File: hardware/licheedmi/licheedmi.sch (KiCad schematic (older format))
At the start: 74 parts, among them J1 Conn_01x09, J2 HDMI_A_PCB, J3 LicheePiNano_LCD, J4 HDMI_A, J5 USB_C_Receptacle_USB2.0, U1 TDA19988, U2 LicheeNano, U3 TS3DV20812, U4 SC6206B, U5 CH340C

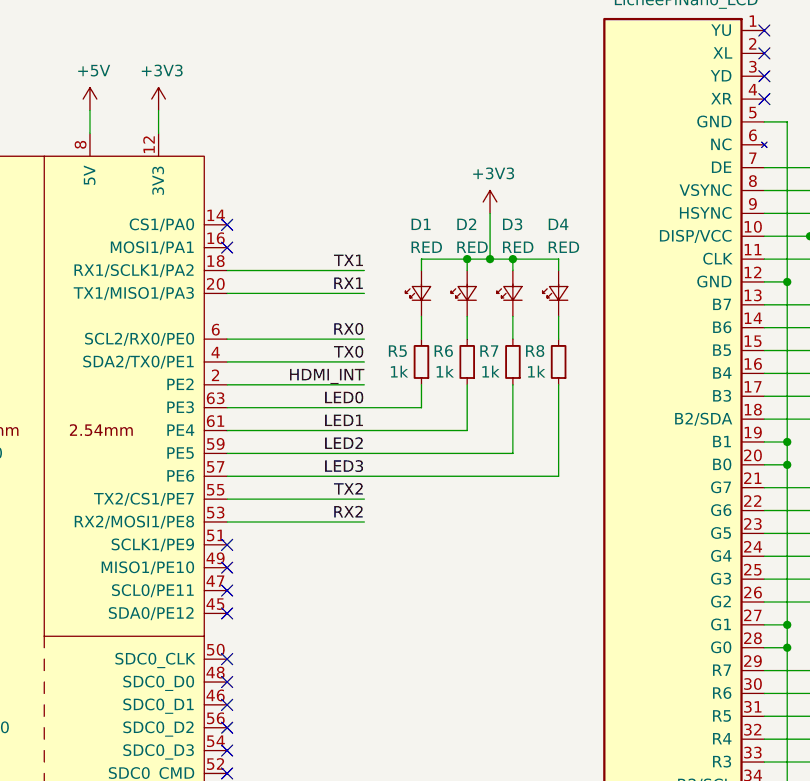
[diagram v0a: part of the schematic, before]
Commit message: pcb: Reroute PCB following footprint flip
Bowtie and complicated via thingies are gone now \o/
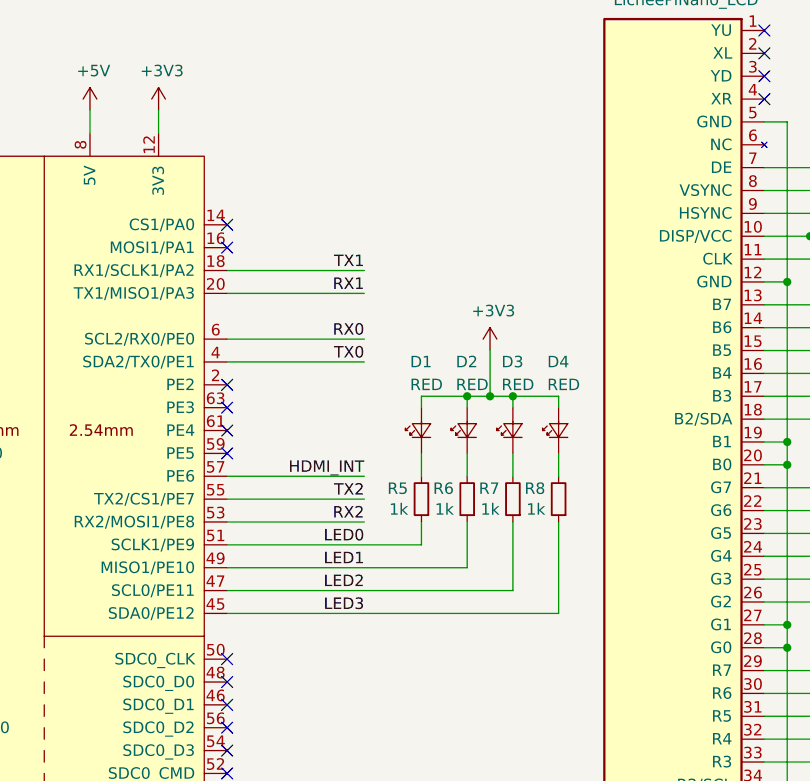
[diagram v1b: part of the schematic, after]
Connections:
- net HDMI_INT: now also U2.57 (PE6); no longer U2.2 (PE2)
- net LED0: now also U2.51 (SCLK1/PE9); no longer U2.63 (PE3)
- net LED1: now also U2.49 (MISO1/PE10); no longer U2.61 (PE4)
- net LED2: now also U2.47 (SCL0/PE11); no longer U2.59 (PE5)
- net LED3: now also U2.45 (SDA0/PE12); no longer U2.57 (PE6)
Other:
- moved on the sheet: D1, D2, D3, D4, R5, R6, R7, R8
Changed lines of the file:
@@
 Wire Wire Line
 	9300 2650 9950 2650
-$Comp
-L hdmizness:LicheeNano U2
-U 1 1 5F223DE5
-P 1750 2600
-F 0 "U2" H 2700 -1000 50  0000 C CNN
-F 1 "LicheeNano" H 2850 -1100 50  0000 C CNN
-F 2 "hdmizness:LicheeNano" H 1500 2650 50  0001 C CNN
-F 3 "${KIPRJMOD}/../../documentation/lichee_nano_8.16_schematic.pdf" H 1500 2650 50  0001 C CNN
-F 4 "C35445" H 1750 2600 50  0001 C CNN "LCSC P/N"
-F 5 "C35445" H 1750 2600 50  0001 C CNN "MFR P/N"
-	1    1750 2600
-	1    0    0    -1
-$EndComp
 Text Label 6200 3650 2    50   ~ 0
 LCD_B3
@@
 RX0
 Wire Wire Line
-	3250 3600 3850 3600
-Text Label 3850 3600 2    50   ~ 0
+	3250 4000 3850 4000
+Text Label 3850 4000 2    50   ~ 0
 HDMI_INT
 $Comp
@@
 Text Label 3850 3200 2    50   ~ 0
 RX1
-Text Label 3850 4000 2    50   ~ 0
+Text Label 3850 4600 2    50   ~ 0
 LED3
-Text Label 3850 3900 2    50   ~ 0
+Text Label 3850 4500 2    50   ~ 0
 LED2
-Text Label 3850 3700 2    50   ~ 0
+Text Label 3850 4300 2    50   ~ 0
 LED0
-Text Label 3850 3800 2    50   ~ 0
+Text Label 3850 4400 2    50   ~ 0
 LED1
 Wire Wire Line
@@
 L Device:R_Small R8
 U 1 1 5F6D2F20
-P 4700 3500
-F 0 "R8" H 4758 3454 50  0000 L CNN
-F 1 "1k" H 4758 3545 50  0000 L CNN
-F 2 "Resistor_SMD:R_0603_1608Metric" H 4700 3500 50  0001 C CNN
-F 3 "~" H 4700 3500 50  0001 C CNN
-F 4 "C380759" H 4700 3500 50  0001 C CNN "LCSC P/N"
-F 5 "SY0603JN1KP" H 4700 3500 50  0001 C CNN "MFR P/N"
-	1    4700 3500
+P 4700 4100
+F 0 "R8" H 4758 4054 50  0000 L CNN
+F 1 "1k" H 4758 4145 50  0000 L CNN
+F 2 "Resistor_SMD:R_0603_1608Metric" H 4700 4100 50  0001 C CNN
+F 3 "~" H 4700 4100 50  0001 C CNN
+F 4 "C380759" H 4700 4100 50  0001 C CNN "LCSC P/N"
+F 5 "SY0603JN1KP" H 4700 4100 50  0001 C CNN "MFR P/N"
+	1    4700 4100
 	-1   0    0    1
 $EndComp
 Wire Wire Line
-	4700 3300 4700 3400
-Wire Wire Line
-	4700 3050 4700 3100
+	4700 3900 4700 4000
+Wire Wire Line
+	4700 3650 4700 3700
 $Comp
 L power:+3V3 #PWR07
 U 1 1 5F89613D
-P 4400 2850
-F 0 "#PWR07" H 4400 2700 50  0001 C CNN
-F 1 "+3V3" H 4415 3023 50  0000 C CNN
-F 2 "" H 4400 2850 50  0001 C CNN
-F 3 "" H 4400 2850 50  0001 C CNN
-	1    4400 2850
-	1    0    0    -1
-$EndComp
-Wire Wire Line
-	4400 3050 4500 3050
-Connection ~ 4400 3050
-Wire Wire Line
-	4400 3050 4400 2850
-Wire Wire Line
-	4500 3050 4700 3050
-Connection ~ 4500 3050
-Wire Wire Line
-	4500 3100 4500 3050
-Wire Wire Line
-	4300 3050 4400 3050
-Connection ~ 4300 3050
-Wire Wire Line
-	4300 3100 4300 3050
-Wire Wire Line
-	4100 3050 4300 3050
-Wire Wire Line
-	4100 3100 4100 3050
-Wire Wire Line
-	4500 3300 4500 3400
-Wire Wire Line
-	4300 3300 4300 3400
-Wire Wire Line
-	4100 3300 4100 3400
+P 4400 3450
+F 0 "#PWR07" H 4400 3300 50  0001 C CNN
+F 1 "+3V3" H 4415 3623 50  0000 C CNN
+F 2 "" H 4400 3450 50  0001 C CNN
+F 3 "" H 4400 3450 50  0001 C CNN
+	1    4400 3450
+	1    0    0    -1
+$EndComp
+Wire Wire Line
+	4400 3650 4500 3650
+Connection ~ 4400 3650
+Wire Wire Line
+	4400 3650 4400 3450
+Wire Wire Line
+	4500 3650 4700 3650
+Connection ~ 4500 3650
+Wire Wire Line
+	4500 3700 4500 3650
+Wire Wire Line
+	4300 3650 4400 3650
+Connection ~ 4300 3650
+Wire Wire Line
+	4300 3700 4300 3650
+Wire Wire Line
+	4100 3650 4300 3650
+Wire Wire Line
+	4100 3700 4100 3650
+Wire Wire Line
+	4500 3900 4500 4000
+Wire Wire Line
+	4300 3900 4300 4000
+Wire Wire Line
+	4100 3900 4100 4000
 $Comp
 L Device:LED_Small D1
 U 1 1 5F6D3496
-P 4100 3200
-F 0 "D1" V 4400 3250 50  0000 R CNN
-F 1 "RED" V 4300 3250 50  0000 R CNN
-F 2 "LED_SMD:LED_0603_1608Metric" V 4100 3200 50  0001 C CNN
-F 3 "~" V 4100 3200 50  0001 C CNN
-F 4 "C157741" H 4100 3200 50  0001 C CNN "LCSC P/N"
-F 5 "LTST-C193KRKT-5A" H 4100 3200 50  0001 C CNN "MFR P/N"
-	1    4100 3200
+P 4100 3800
+F 0 "D1" V 4400 3850 50  0000 R CNN
+F 1 "RED" V 4300 3850 50  0000 R CNN
+F 2 "LED_SMD:LED_0603_1608Metric" V 4100 3800 50  0001 C CNN
+F 3 "~" V 4100 3800 50  0001 C CNN
+F 4 "C157741" H 4100 3800 50  0001 C CNN "LCSC P/N"
+F 5 "LTST-C193KRKT-5A" H 4100 3800 50  0001 C CNN "MFR P/N"
+	1    4100 3800
 	0    -1   -1   0
 $EndComp
@@
 L Device:R_Small R7
 U 1 1 5F6D2C74
-P 4500 3500
-F 0 "R7" H 4558 3454 50  0000 L CNN
-F 1 "1k" H 4558 3545 50  0000 L CNN
-F 2 "Resistor_SMD:R_0603_1608Metric" H 4500 3500 50  0001 C CNN
-F 3 "~" H 4500 3500 50  0001 C CNN
-F 4 "C380759" H 4500 3500 50  0001 C CNN "LCSC P/N"
-F 5 "SY0603JN1KP" H 4500 3500 50  0001 C CNN "MFR P/N"
-	1    4500 3500
+P 4500 4100
+F 0 "R7" H 4558 4054 50  0000 L CNN
+F 1 "1k" H 4558 4145 50  0000 L CNN
+F 2 "Resistor_SMD:R_0603_1608Metric" H 4500 4100 50  0001 C CNN
+F 3 "~" H 4500 4100 50  0001 C CNN
+F 4 "C380759" H 4500 4100 50  0001 C CNN "LCSC P/N"
+F 5 "SY0603JN1KP" H 4500 4100 50  0001 C CNN "MFR P/N"
+	1    4500 4100
 	-1   0    0    1
 $EndComp
@@
 L Device:R_Small R6
 U 1 1 5F6D21F3
-P 4300 3500
-F 0 "R6" H 4358 3454 50  0000 L CNN
-F 1 "1k" H 4358 3545 50  0000 L CNN
-F 2 "Resistor_SMD:R_0603_1608Metric" H 4300 3500 50  0001 C CNN
-F 3 "~" H 4300 3500 50  0001 C CNN
-F 4 "C380759" H 4300 3500 50  0001 C CNN "LCSC P/N"
-F 5 "SY0603JN1KP" H 4300 3500 50  0001 C CNN "MFR P/N"
-	1    4300 3500
+P 4300 4100
+F 0 "R6" H 4358 4054 50  0000 L CNN
+F 1 "1k" H 4358 4145 50  0000 L CNN
+F 2 "Resistor_SMD:R_0603_1608Metric" H 4300 4100 50  0001 C CNN
+F 3 "~" H 4300 4100 50  0001 C CNN
+F 4 "C380759" H 4300 4100 50  0001 C CNN "LCSC P/N"
+F 5 "SY0603JN1KP" H 4300 4100 50  0001 C CNN "MFR P/N"
+	1    4300 4100
 	-1   0    0    1
 $EndComp
@@
 L Device:R_Small R5
 U 1 1 5F6D0AA1
-P 4100 3500
-F 0 "R5" H 4158 3454 50  0000 L CNN
-F 1 "1k" H 4158 3545 50  0000 L CNN
-F 2 "Resistor_SMD:R_0603_1608Metric" H 4100 3500 50  0001 C CNN
-F 3 "~" H 4100 3500 50  0001 C CNN
-F 4 "C380759" H 4100 3500 50  0001 C CNN "LCSC P/N"
-F 5 "SY0603JN1KP" H 4100 3500 50  0001 C CNN "MFR P/N"
-	1    4100 3500
+P 4100 4100
+F 0 "R5" H 4158 4054 50  0000 L CNN
+F 1 "1k" H 4158 4145 50  0000 L CNN
+F 2 "Resistor_SMD:R_0603_1608Metric" H 4100 4100 50  0001 C CNN
+F 3 "~" H 4100 4100 50  0001 C CNN
+F 4 "C380759" H 4100 4100 50  0001 C CNN "LCSC P/N"
+F 5 "SY0603JN1KP" H 4100 4100 50  0001 C CNN "MFR P/N"
+	1    4100 4100
 	-1   0    0    1
 $EndComp
 Wire Wire Line
-	4100 3700 4100 3600
-Wire Wire Line
-	3250 3700 4100 3700
-Wire Wire Line
-	4300 3800 4300 3600
-Wire Wire Line
-	3250 3800 4300 3800
-Wire Wire Line
-	4500 3900 4500 3600
-Wire Wire Line
-	3250 3900 4500 3900
-Wire Wire Line
-	4700 4000 4700 3600
-Wire Wire Line
-	3250 4000 4700 4000
+	4100 4300 4100 4200
+Wire Wire Line
+	3250 4300 4100 4300
+Wire Wire Line
+	4300 4400 4300 4200
+Wire Wire Line
+	3250 4400 4300 4400
+Wire Wire Line
+	4500 4500 4500 4200
+Wire Wire Line
+	3250 4500 4500 4500
+Wire Wire Line
+	4700 4600 4700 4200
+Wire Wire Line
+	3250 4600 4700 4600
 NoConn ~ 3250 2900
-NoConn ~ 3250 3000
-NoConn ~ 3250 4300
-NoConn ~ 3250 4400
-NoConn ~ 3250 4500
-NoConn ~ 3250 4600
+NoConn ~ 3250 3600
 $Comp
 L hdmizness:SC6206B U4
@@
 L Device:LED_Small D2
 U 1 1 613C01A5
-P 4300 3200
-F 0 "D2" V 4600 3250 50  0000 R CNN
-F 1 "RED" V 4500 3250 50  0000 R CNN
-F 2 "LED_SMD:LED_0603_1608Metric" V 4300 3200 50  0001 C CNN
-F 3 "~" V 4300 3200 50  0001 C CNN
-F 4 "C157741" H 4300 3200 50  0001 C CNN "LCSC P/N"
-F 5 "LTST-C193KRKT-5A" H 4300 3200 50  0001 C CNN "MFR P/N"
-	1    4300 3200
+P 4300 3800
+F 0 "D2" V 4600 3850 50  0000 R CNN
+F 1 "RED" V 4500 3850 50  0000 R CNN
+F 2 "LED_SMD:LED_0603_1608Metric" V 4300 3800 50  0001 C CNN
+F 3 "~" V 4300 3800 50  0001 C CNN
+F 4 "C157741" H 4300 3800 50  0001 C CNN "LCSC P/N"
+F 5 "LTST-C193KRKT-5A" H 4300 3800 50  0001 C CNN "MFR P/N"
+	1    4300 3800
 	0    -1   -1   0
 $EndComp
@@
 L Device:LED_Small D3
 U 1 1 613C082E
-P 4500 3200
-F 0 "D3" V 4800 3250 50  0000 R CNN
-F 1 "RED" V 4700 3250 50  0000 R CNN
-F 2 "LED_SMD:LED_0603_1608Metric" V 4500 3200 50  0001 C CNN
-F 3 "~" V 4500 3200 50  0001 C CNN
-F 4 "C157741" H 4500 3200 50  0001 C CNN "LCSC P/N"
-F 5 "LTST-C193KRKT-5A" H 4500 3200 50  0001 C CNN "MFR P/N"
-	1    4500 3200
+P 4500 3800
+F 0 "D3" V 4800 3850 50  0000 R CNN
+F 1 "RED" V 4700 3850 50  0000 R CNN
+F 2 "LED_SMD:LED_0603_1608Metric" V 4500 3800 50  0001 C CNN
+F 3 "~" V 4500 3800 50  0001 C CNN
+F 4 "C157741" H 4500 3800 50  0001 C CNN "LCSC P/N"
+F 5 "LTST-C193KRKT-5A" H 4500 3800 50  0001 C CNN "MFR P/N"
+	1    4500 3800
 	0    -1   -1   0
 $EndComp
@@
 L Device:LED_Small D4
 U 1 1 613C0C7E
-P 4700 3200
-F 0 "D4" V 5000 3250 50  0000 R CNN
-F 1 "RED" V 4900 3250 50  0000 R CNN
-F 2 "LED_SMD:LED_0603_1608Metric" V 4700 3200 50  0001 C CNN
-F 3 "~" V 4700 3200 50  0001 C CNN
-F 4 "C157741" H 4700 3200 50  0001 C CNN "LCSC P/N"
-F 5 "LTST-C193KRKT-5A" H 4700 3200 50  0001 C CNN "MFR P/N"
-	1    4700 3200
+P 4700 3800
+F 0 "D4" V 5000 3850 50  0000 R CNN
+F 1 "RED" V 4900 3850 50  0000 R CNN
+F 2 "LED_SMD:LED_0603_1608Metric" V 4700 3800 50  0001 C CNN
+F 3 "~" V 4700 3800 50  0001 C CNN
+F 4 "C157741" H 4700 3800 50  0001 C CNN "LCSC P/N"
+F 5 "LTST-C193KRKT-5A" H 4700 3800 50  0001 C CNN "MFR P/N"
+	1    4700 3800
 	0    -1   -1   0
 $EndComp
@@
 	5700 2450 5700 3150
 Connection ~ 5700 3150
+$Comp
+L hdmizness:LicheeNano U2
+U 1 1 5F223DE5
+P 1750 2600
+F 0 "U2" H 2700 -1000 50  0000 C CNN
+F 1 "LicheeNano" H 2850 -1100 50  0000 C CNN
+F 2 "hdmizness:LicheeNano" H 1500 2650 50  0001 C CNN
+F 3 "${KIPRJMOD}/../../documentation/lichee_nano_8.16_schematic.pdf" H 1500 2650 50  0001 C CNN
+F 4 "C35445" H 1750 2600 50  0001 C CNN "LCSC P/N"
+F 5 "C35445" H 1750 2600 50  0001 C CNN "MFR P/N"
+	1    1750 2600
+	1    0    0    -1
+$EndComp
+NoConn ~ 3250 3700
+NoConn ~ 3250 3800
+NoConn ~ 3250 3900
+NoConn ~ 3250 3000
 $EndSCHEMATC

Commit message: sch: Wire I2S
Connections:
- net HDMI_INT: now also U2.59 (PE5); no longer U2.57 (PE6)
- net I2S_BCLK: now reaches U1.23 (ACLK)
- net I2S_BCLK: now also U2.63 (PE3)
- net I2S_LRCLK: now reaches U1.24 (AP0)
- net I2S_LRCLK: now also U2.61 (PE4)
- net I2S_DO: now reaches U1.25 (AP1)
- net I2S_DO: now also U2.57 (PE6)
- no-connect marks 53 -> 47
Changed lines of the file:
@@
 EESchema Schematic File Version 4
+LIBS:licheedmi-cache
 EELAYER 30 0
 EELAYER END
@@
 NoConn ~ 5600 5850
 NoConn ~ 5600 5950
-NoConn ~ 7000 5850
-NoConn ~ 7000 5950
-NoConn ~ 7000 6050
 NoConn ~ 7000 6150
 NoConn ~ 7000 6250
@@
 RX0
 Wire Wire Line
-	3250 4000 3850 4000
-Text Label 3850 4000 2    50   ~ 0
+	3250 3900 3850 3900
+Text Label 3850 3900 2    50   ~ 0
 HDMI_INT
 $Comp
@@
 	1    0    0    -1
 $EndComp
-NoConn ~ 3250 3700
-NoConn ~ 3250 3800
-NoConn ~ 3250 3900
 NoConn ~ 3250 3000
+Wire Wire Line
+	3850 3700 3250 3700
+Text Label 3850 3700 2    50   ~ 0
+I2S_BCLK
+Wire Wire Line
+	3850 3800 3250 3800
+Text Label 3850 3800 2    50   ~ 0
+I2S_LRCLK
+Wire Wire Line
+	3850 4000 3250 4000
+Text Label 3850 4000 2    50   ~ 0
+I2S_DO
+Wire Wire Line
+	6400 5850 7000 5850
+Text Label 6400 5850 0    50   ~ 0
+I2S_BCLK
+Wire Wire Line
+	6400 5950 7000 5950
+Text Label 6400 5950 0    50   ~ 0
+I2S_LRCLK
+Wire Wire Line
+	6400 6050 7000 6050
+Text Label 6400 6050 0    50   ~ 0
+I2S_DO
 $EndSCHEMATC

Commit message: sch: Replace TDA19988 with SiI9022A (wip)
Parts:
- removed R4: 10k, Resistor_SMD:R_0603_1608Metric, symbol Device:R_Small
- removed U1: TDA19988, Package_DFN_QFN:QFN-64-1EP_9x9mm_P0.5mm_EP4.7x4.7mm, symbol hdmizness:TDA19988
- added U?: SiI9022A, hdmizness:QFN-72-1EP_10x10mm_P0.5mm_EP4.7x4.7mm_ThermalVias, symbol hdmizness:SiI9022A
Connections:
- net CPU_SCL: now also U?.1 (CSCL)
- net CPU_SDA: now also U?.2 (CSDA)
- net GND: now also U?.10 (D18), U?.11 (D17), U?.13 (D16), U?.20 (D9), U?.23 (D8), U?.30 (D2), U?.31 (D1), U?.32 (D0), U?.43 (CGND), U?.57 (IOGND), U?.63 (AGND), U?.EP (GND)
- net HD0_N: now also U?.61 (TX0_N)
- net HD0_P: now also U?.62 (TX0_P)
- net HD1_N: now also U?.64 (TX1_N)
- net HD1_P: now also U?.65 (TX1_P)
- net HD2_N: now also U?.67 (TX2_N)
- net HD2_P: now also U?.68 (TX2_P)
- net HDCEC: now also U?.71 (CEC_A)
- net HDC_N: now also U?.58 (TXC_N)
- net HDC_P: now also U?.59 (TXC_P)
- net HDC_PCB_N: no longer J2.12 (CK-)
- net HDMI_INT: now also U?.52 (INT)
- net HDSCL: now also U?.49 (DSCL)
- net HDSDA: now also U?.48 (DSDA)
- net HPD: now also U?.54 (HPD)
- net I2S_BCLK: now also U?.45 (I2S_SCK)
- net I2S_DO: now also U?.41 (I2S_SD0)
- net I2S_LRCLK: now also U?.44 (I2S_WS)
- net LCD_B3: now also U?.9 (D19)
- net LCD_B4: now also U?.8 (D20)
- net LCD_B5: now also U?.7 (D21)
- net LCD_B6: now also U?.6 (D22)
- net LCD_B7: now also U?.4 (D23)
- net LCD_CLK: now also U?.22 (PCLK)
- net LCD_DE: now also U?.33 (DE)
- net LCD_G2: now also U?.19 (D10)
- net LCD_G3: now also U?.18 (D11)
- net LCD_G4: now also U?.17 (D12)
- net LCD_G5: now also U?.16 (D13)
- net LCD_G6: now also U?.15 (D14)
- net LCD_G7: now also U?.14 (D15)
- net LCD_HSYNC: now also U?.34 (HSYNC)
- net LCD_R3: now also U?.29 (D3)
- net LCD_R4: now also U?.28 (D4)
- net LCD_R5: now also U?.27 (D5)
- net LCD_R6: now also U?.25 (D6)
- net LCD_R7: now also U?.24 (D7)
- net LCD_VSYNC: now also U?.35 (VSYNC)
- net at R16.1: now also U?.56 (EXT_SWING)
- net at R3.2: now also U?.72 (I2C_A2)
- net HDMI_CDC: now reaches U2.2 (PE2)
- net HDMI_CDC: now also U?.50 (CDC_D)
- no-connect marks 47 -> 48
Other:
- note added: "Base addresses:\n- TPI Core: 0b01110x10 = 0x72\n- CEC Core: 0b11000x00 = 0xC0\nLicheeNano has the touch controller at 0x48"
- note removed: "Base addresses:\n- HDMI Core: 0b11100xx = 0x70\n- CEC Core: 0b01101xx = 0x34\nLicheeNano has the touch controller at 0x48"
- moved on the sheet: J3

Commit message: sch: Use 1.2V LDO for SiI and fix auxilary signals
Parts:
- removed U4: SC6206B, Package_TO_SOT_SMD:SOT-23, symbol hdmizness:SC6206B
- added U4: TLV74312PDBVR, Package_TO_SOT_SMD:TSOT-23-5, symbol hdmizness:TLV74312PDBVR
- R16: value 10k -> 4k3; LCSC P/N C98220 -> C23159; MFR P/N RC0603FR-0710KL -> 0603WAF4301T5E
- TP12: value VDDC -> CVCC12
- TP13: value +1V8 -> +1V2
- TP14: value VDDATX -> IOVCC
- TP15: value VDDAPLL -> AVCC12
- U1: renamed from U?; LCSC P/N (none) -> C369565; MFR P/N (none) -> SII9022ACNU
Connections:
- net VDDA is gone; now on net CVCC12: C2.1, C3.1, C4.1, C5.1, C6.1, C7.1, FB1.1, TP12.1
- net VDDAPLL is gone; now on net AVCC12: C14.1, C15.1, FB3.1, TP15.1
- net VDDATX is gone; now on net IOVCC: C10.1, C11.1, C12.1, FB2.1, TP14.1
- net +3V3: now also FB2.2, U4.1 (IN), U4.3 (EN)
- net GND: now also U1.55 (RSVDL), U1.69 (IO_SEL), U1.70 (VDDQ), U4.2 (GND)
- net HDC_PCB_N: now also J2.12 (CK-)
- net CVCC12: now reaches U1.12 (CVCC12)
- net CVCC12: now also U1.26 (CVCC12), U1.42 (CVCC12), U1.47 (CVCC12), U1.5 (CVCC12), U1.53 (CVCC12)
- net IOVCC: now reaches U1.21 (IOVCC)
- net IOVCC: now also U1.3 (IOVCC), U1.46 (IOVCC)
- net HDMI_~RST: now reaches U1.51 (~RST)
- net HDMI_~RST: now also U2.16 (MOSI1/PA1)
- net AVCC12: now reaches U1.60 (AVCC12)
- net AVCC12: now also U1.66 (AVCC12)
- net +1V8 renamed +1V2
- net +1V2: now also U4.5 (OUT); no longer FB2.2
- no-connect marks 48 -> 47
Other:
- moved on the sheet: C8, C9, TP12

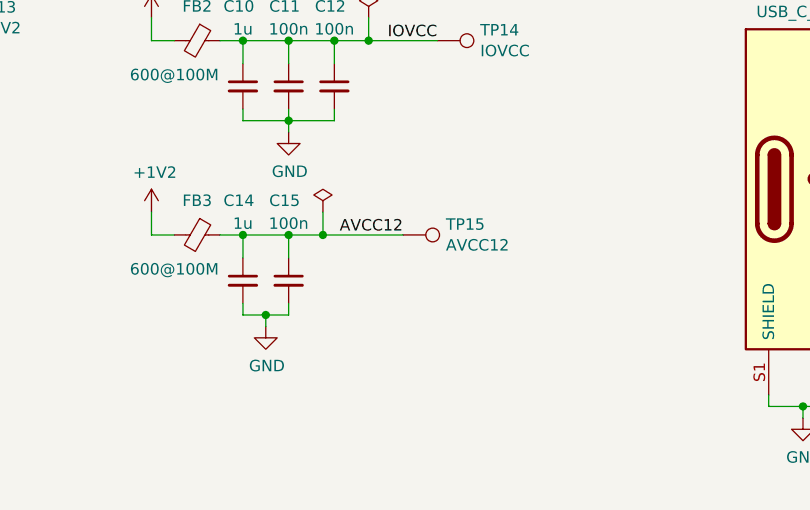
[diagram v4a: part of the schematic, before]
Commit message: sch: Add extra decoupling cap on AVCC line
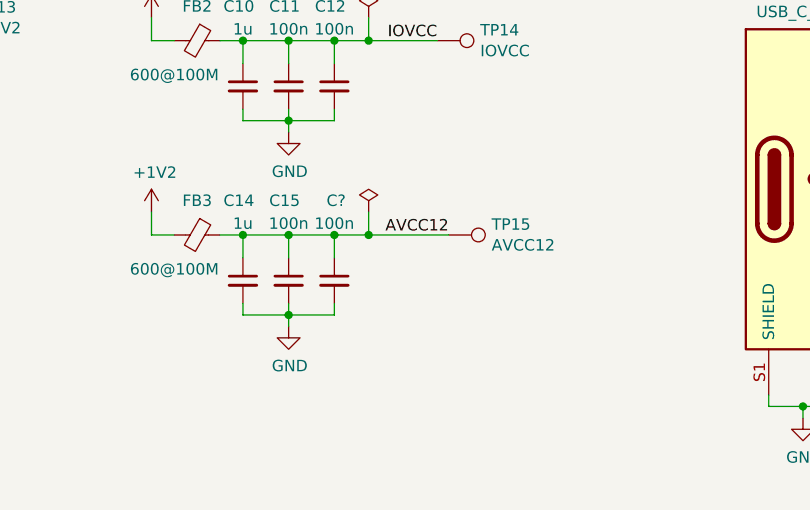
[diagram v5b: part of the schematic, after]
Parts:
- added C?: 100n, Capacitor_SMD:C_0603_1608Metric, symbol Device:C_Small
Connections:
- net AVCC12: now also C?.1
- net GND: now also C?.2
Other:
- moved on the sheet: TP15
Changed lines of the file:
@@
 	1    0    0    -1
 $EndComp
-Text Label 4900 9750 2    50   ~ 0
+Text Label 5100 9750 2    50   ~ 0
 AVCC12
 $Comp
 L power:GND #PWR036
 U 1 1 601EC6F9
-P 4300 10150
-F 0 "#PWR036" H 4300 9900 50  0001 C CNN
-F 1 "GND" H 4305 9977 50  0000 C CNN
-F 2 "" H 4300 10150 50  0001 C CNN
-F 3 "" H 4300 10150 50  0001 C CNN
-	1    4300 10150
+P 4400 10150
+F 0 "#PWR036" H 4400 9900 50  0001 C CNN
+F 1 "GND" H 4405 9977 50  0000 C CNN
+F 2 "" H 4400 10150 50  0001 C CNN
+F 3 "" H 4400 10150 50  0001 C CNN
+	1    4400 10150
 	1    0    0    -1
 $EndComp
@@
 	4200 10050 4200 10100
 Wire Wire Line
-	4200 10100 4300 10100
-Wire Wire Line
 	4400 10100 4400 10050
 Wire Wire Line
-	4300 10150 4300 10100
+	4400 10150 4400 10100
 $Comp
 L Device:C_Small C2
@@
 L Connector:TestPoint TP15
 U 1 1 61568FAC
-P 4900 9750
-F 0 "TP15" V 4854 9938 50  0000 L CNN
-F 1 "AVCC12" V 4945 9938 50  0000 L CNN
-F 2 "TestPoint:TestPoint_Pad_D1.0mm" H 5100 9750 50  0001 C CNN
-F 3 "~" H 5100 9750 50  0001 C CNN
-	1    4900 9750
+P 5100 9750
+F 0 "TP15" V 5054 9938 50  0000 L CNN
+F 1 "AVCC12" V 5145 9938 50  0000 L CNN
+F 2 "TestPoint:TestPoint_Pad_D1.0mm" H 5300 9750 50  0001 C CNN
+F 3 "~" H 5300 9750 50  0001 C CNN
+	1    5100 9750
 	0    1    1    0
 $EndComp
@@
 	4600 8900 4750 8900
 Wire Wire Line
-	4400 9750 4550 9750
+	4400 9750 4600 9750
 Wire Wire Line
 	4400 9250 4600 9250
-Connection ~ 4300 10100
-Wire Wire Line
-	4300 10100 4400 10100
 $Comp
 L Connector_Generic:Conn_01x09 J1
@@
 L power:PWR_FLAG #FLG0104
 U 1 1 61B76D89
-P 4550 9650
-F 0 "#FLG0104" H 4550 9725 50  0001 C CNN
-F 1 "PWR_FLAG" H 4550 9823 50  0001 C CNN
-F 2 "" H 4550 9650 50  0001 C CNN
-F 3 "~" H 4550 9650 50  0001 C CNN
-	1    4550 9650
-	1    0    0    -1
-$EndComp
-Wire Wire Line
-	4550 9650 4550 9750
-Connection ~ 4550 9750
-Wire Wire Line
-	4550 9750 4900 9750
+P 4750 9650
+F 0 "#FLG0104" H 4750 9725 50  0001 C CNN
+F 1 "PWR_FLAG" H 4750 9823 50  0001 C CNN
+F 2 "" H 4750 9650 50  0001 C CNN
+F 3 "~" H 4750 9650 50  0001 C CNN
+	1    4750 9650
+	1    0    0    -1
+$EndComp
+Wire Wire Line
+	4750 9650 4750 9750
+Connection ~ 4750 9750
+Wire Wire Line
+	4750 9750 5100 9750
 Wire Wire Line
 	4750 8800 4750 8900
@@
 	1    0    0    -1
 $EndComp
+$Comp
+L Device:C_Small C?
+U 1 1 5FD5762A
+P 4600 9950
+F 0 "C?" H 4650 10300 50  0000 R CNN
+F 1 "100n" H 4600 10200 50  0000 C CNN
+F 2 "Capacitor_SMD:C_0603_1608Metric" H 4600 9950 50  0001 C CNN
+F 3 "~" H 4600 9950 50  0001 C CNN
+F 4 "C1591" H 4600 9950 50  0001 C CNN "LCSC P/N"
+F 5 "CL10B104KB8NNNC" H 4600 9950 50  0001 C CNN "MFR P/N"
+	1    4600 9950
+	1    0    0    -1
+$EndComp
+Wire Wire Line
+	4600 9850 4600 9750
+Connection ~ 4600 9750
+Wire Wire Line
+	4600 9750 4750 9750
+Wire Wire Line
+	4400 10100 4600 10100
+Wire Wire Line
+	4600 10100 4600 10050
+Connection ~ 4400 10100
+Wire Wire Line
+	4200 10100 4400 10100
 $EndSCHEMATC
